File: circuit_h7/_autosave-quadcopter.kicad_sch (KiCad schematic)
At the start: 109 parts, among them J10 Conn_01x01_Female, J11 Conn_01x04_Male, J12 Conn_01x04_Male, J13 Conn_01x01_Female, J16 Conn_01x01_Female, J17 Conn_01x01_Female, J18 USB_C_Receptacle_USB2.0, J19 Conn_01x08_Male, J21 Conn_01x01_Female, J22 Conn_01x01_Female, J23 Conn_01x01_Female, J24 Conn_01x01_Female, J25 Conn_01x01_Female, J26 Conn_01x01_Female, J28 Conn_01x01_Female, J29 Conn_01x01_Female, J3 Conn_01x01_Female, J30 Conn_01x01_Female, J31 Conn_01x01_Female, J32 Conn_01x01_Female, J33 Conn_01x01_Female, J37 Conn_01x01_Female, J4 Conn_01x01_Female, J40 Conn_01x01_Female, J41 Conn_01x01_Female, J42 Conn_01x01_Female, J43 Conn_01x01_Female, J44 Conn_01x01_Female, J45 Conn_01x01_Female, J47 Conn_01x01_Female, J48 Conn_01x01_Female, J49 Conn_01x01_Female, J5 Conn_Coaxial, J50 Conn_01x01_Female, J6 Conn_01x06_Male, J7 Conn_01x01_Female, J8 Conn_01x01_Female, J9 Conn_01x01_Female, Q1 AO3400A, SW1 SW_DIP_x01, U1 STM32F103VDHx, U2 ICM-42605, U3 DPS310, U4 3V3, U5 EUP3458 1.2A, 30V max input, 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, U6 2450FM07D0034T, U7 W25Q80DVUXIE TR (16M), U8 SX1281, U9 5v, 500mA, Y1 16M, Y2 52Mhz, 12pF

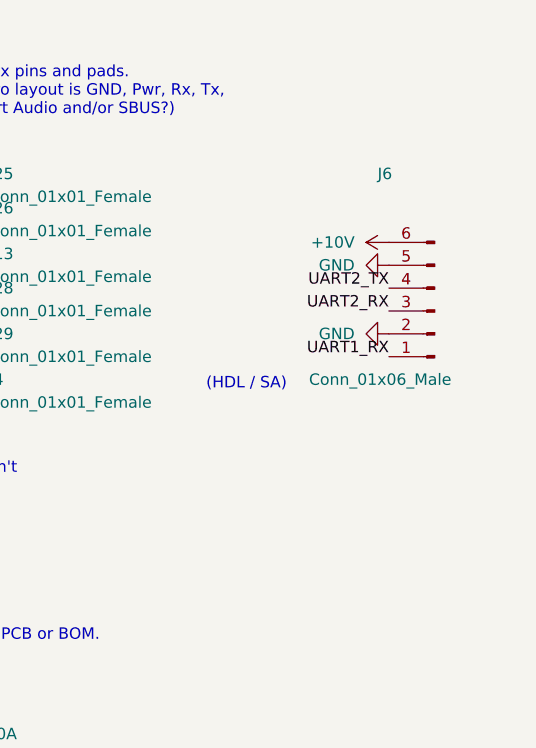
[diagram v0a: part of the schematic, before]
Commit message: Refactored baro/alt module, including applying calibration and temp comp
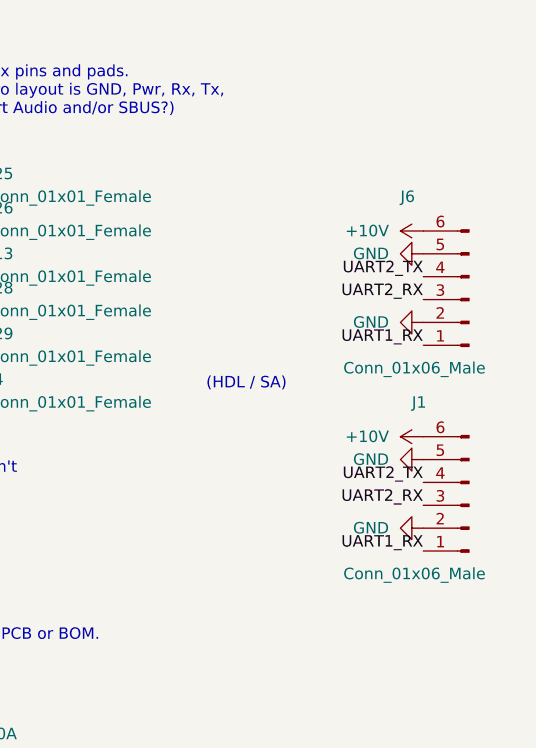
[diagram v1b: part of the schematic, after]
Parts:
- added J1: Conn_01x06_Male, Connector_JST:JST_SH_BM06B-SRSS-TB_1x06-1MP_P1.00mm_Vertical, symbol Connector:Conn_01x06_Male
- U7: footprint Anyleaf_Shared:USON-8_2.0x3.0mm_P0.5mm -> Package_SON:WSON-8-1EP_6x5mm_P1.27mm_EP3.4x4.3mm; Digikey W25Q80DVUXIETR-ND -> (none)
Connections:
- net +10V: now also J1.6 (Pin_6)
- net GND: now also J1.2 (Pin_2), J1.5 (Pin_5)
- net UART1_RX: now also J1.1 (Pin_1)
- net UART2_RX: now also J1.3 (Pin_3)
- net UART2_TX: now also J1.4 (Pin_4)
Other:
- moved on the sheet: J6
